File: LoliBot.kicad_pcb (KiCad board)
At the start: 2 copper layers, 146 x 100 mm, 27 parts, among them J1 LOLINBATT, J10 LEFT-MOTOR, J2 APA106, J3 SERVO1, J4 RIGHT, J5 LEFT, J6 MPU-9250, J7 APA106, J8 APA106, J9 RIGHT-MOTOR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

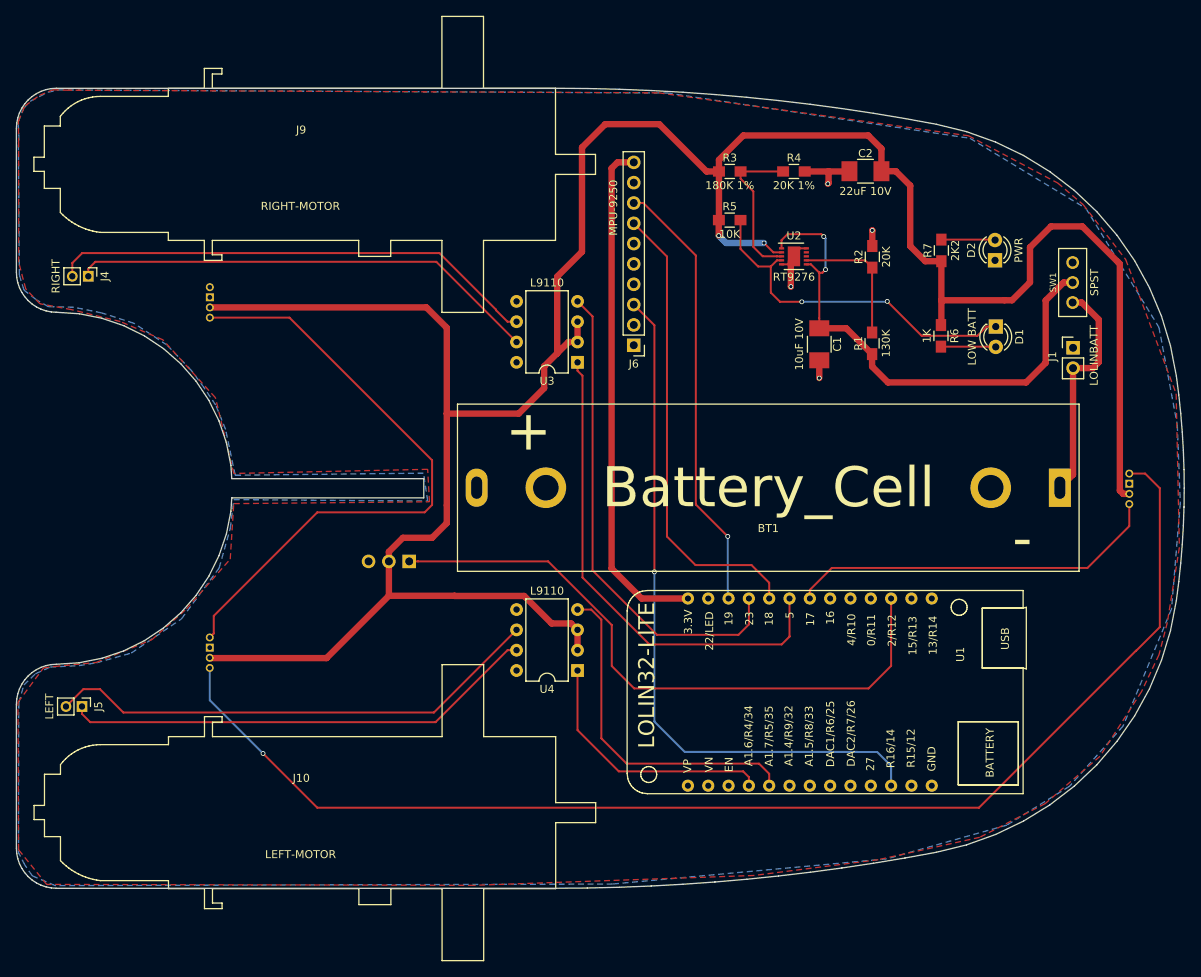
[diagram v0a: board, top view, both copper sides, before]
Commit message: Added Mounting brackets and IR sensor
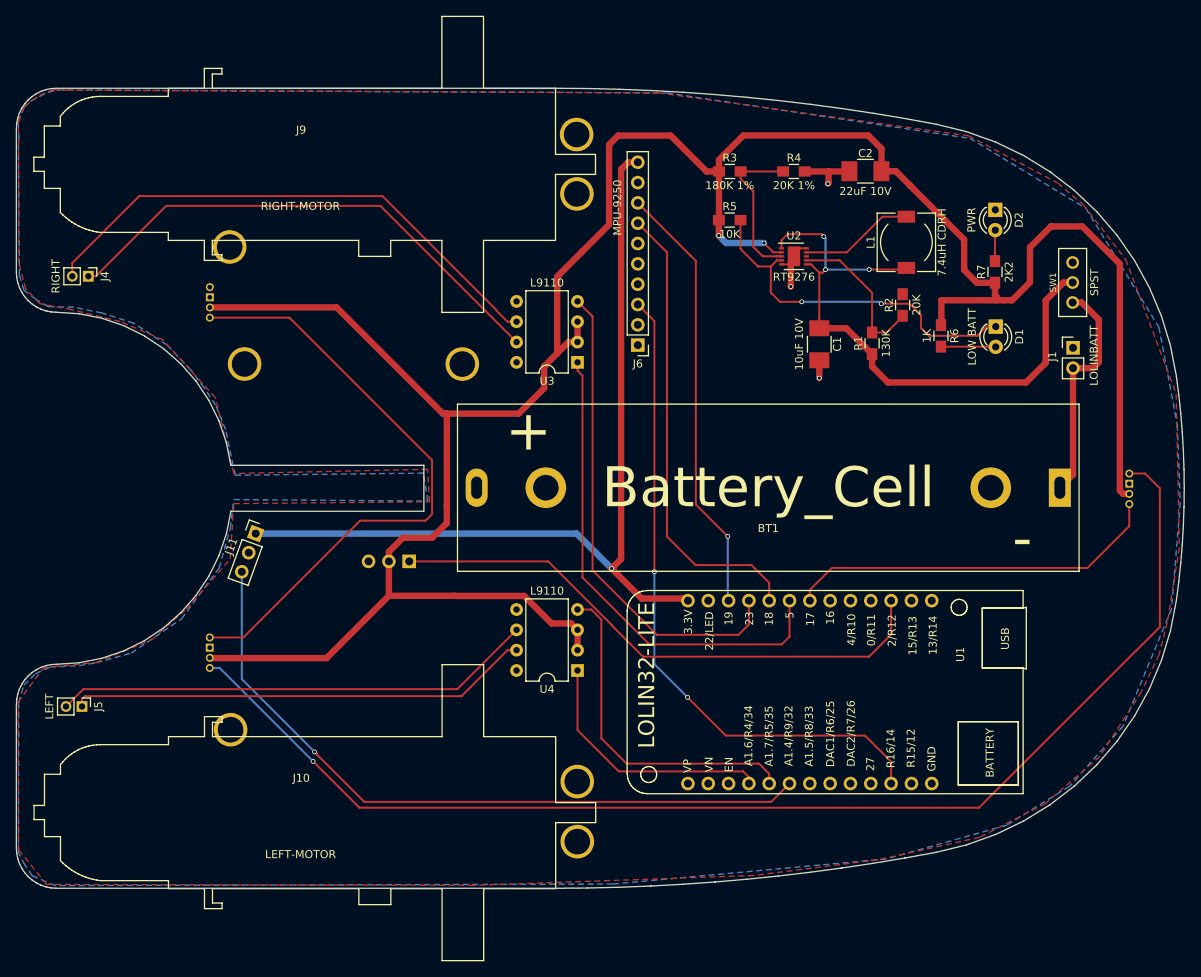
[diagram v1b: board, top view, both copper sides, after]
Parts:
- added J11: REFLECT_, Pin_Headers:Pin_Header_Straight_1x03_Pitch2.54mm, F.Cu at (80.9, 94.9)
- added J12: MECH, Mounting_Holes:MountingHole_3.2mm_M3_Pad, F.Cu at (106.7, 73.7)
- added J13: MECH, Mounting_Holes:MountingHole_3.2mm_M3_Pad, F.Cu at (121.1, 125.9)
- added J14: MECH, Mounting_Holes:MountingHole_3.2mm_M3_Pad, F.Cu at (121.1, 133.4)
- added J15: MECH, Mounting_Holes:MountingHole_3.2mm_M3_Pad, F.Cu at (79.5, 73.7)
- added J16: MECH, Mounting_Holes:MountingHole_3.2mm_M3_Pad, F.Cu at (77.8, 119.4)
- added J17: MECH, Mounting_Holes:MountingHole_3.2mm_M3_Pad, F.Cu at (77.6, 59.1)
- added J18: MECH, Mounting_Holes:MountingHole_3.2mm_M3_Pad, F.Cu at (121.0, 52.5)
- added J19: MECH, Mounting_Holes:MountingHole_3.2mm_M3_Pad, F.Cu at (121.0, 45.0)
- added L1: 7.4uH CDRH, Choke_SMD:Choke_SMD_7.3x7.3_H3.5, F.Cu at (162.2, 58.5)
- moved R7 7.22 mm to (173.3, 62.2)
- moved R2 7.11 mm to (161.8, 66.4)
- moved D2 6.31 mm to (173.3, 54.5), turned to 270 degrees
- moved J6 0.51 mm to (128.7, 71.4)
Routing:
- net /IO32: track 0.00 -> 89.2 mm, vias 0 -> 1
- net +3V3: track 64.2 -> 110.2 mm, vias 0 -> 1
- net Net-(L1-Pad2): track 0.00 -> 14.3 mm
- net Net-(C1-Pad1): track 66.1 -> 76.3 mm, vias 2 -> 3
- net /IO2: track 79.4 -> 70.9 mm
- net +5V: track 322.8 -> 316.4 mm
- net Net-(J4-Pad2): track 61.3 -> 67.2 mm
- net Net-(J4-Pad1): track 59.0 -> 64.2 mm
- net /INT: track 87.5 -> 83.2 mm, vias 1 -> 2
- net Net-(R1-Pad2): track 16.7 -> 19.6 mm
- net Net-(D2-Pad2): track 6.73 -> 3.89 mm
- net Net-(J5-Pad2): track 62.7 -> 60.3 mm
- net Net-(J2-Pad4): track 159.6 -> 157.3 mm
- net GND: track 20.0 -> 18.0 mm, vias 4 -> 3
- net Net-(J5-Pad1): track 59.4 -> 57.8 mm
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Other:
- outline, holes or cut-outs redrawn

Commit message: Updated footprint
Improved motor driver positions.
Rotated acel to match x/y directions
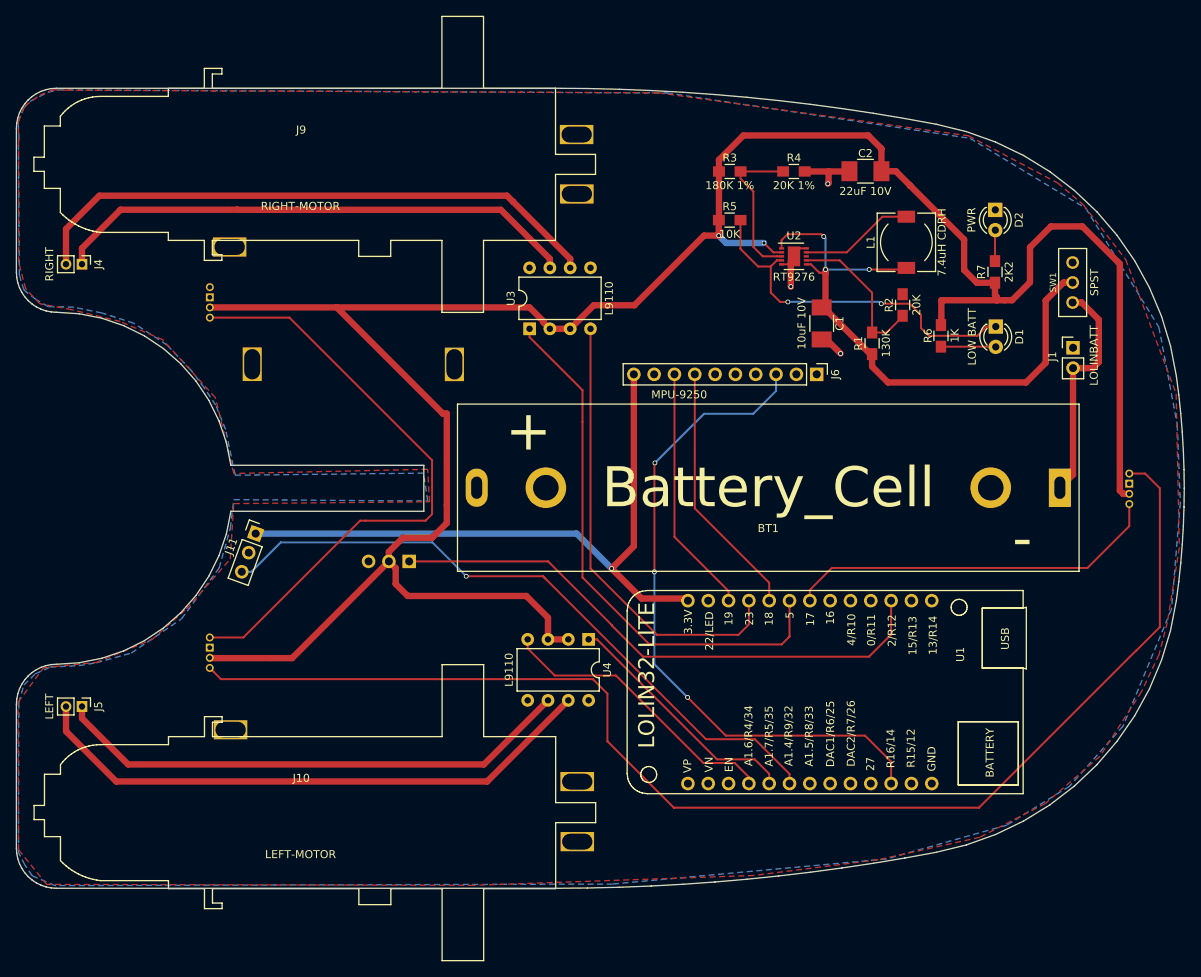
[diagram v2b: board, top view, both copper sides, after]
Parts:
- moved J6 22.7 mm to (151.0, 75.0), turned to 270 degrees
- moved U3 7.32 mm to (115.1, 69.3), turned to 90 degrees
- moved U4 4.13 mm to (122.5, 108.1), turned to 270 degrees
- moved C1 2.62 mm to (151.6, 68.7)
- moved J4 1.70 mm to (59.2, 61.3)
- moved J12 0.99 mm to (105.7, 73.8)
- moved J15 0.96 mm to (80.5, 73.8)
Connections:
- U4 pad 1: /IO34 -> /IO35
- U4 pad 4: /IO35 -> /IO34
- U4 pad 6: Net-(J5-Pad2) -> Net-(J5-Pad1)
- U4 pad 7: Net-(J5-Pad1) -> Net-(J5-Pad2)
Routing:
- net +3V3: track 110.2 -> 82.8 mm
- net /IO18: track 57.8 -> 31.9 mm
- net /IO19: track 54.2 -> 31.2 mm, vias 1 -> 0
- net +5V: track 316.4 -> 300.0 mm
- net Net-(J5-Pad2): track 60.3 -> 72.7 mm
- net /IO35: track 42.6 -> 31.0 mm
- net Net-(J5-Pad1): track 57.8 -> 65.4 mm
- net /IO5: track 61.7 -> 68.3 mm
- net Net-(J4-Pad2): track 67.2 -> 73.5 mm
- net /IO32: track 89.2 -> 83.4 mm
- net /IO34: track 32.4 -> 36.5 mm
- net /IO23: track 61.1 -> 57.0 mm
- net Net-(J2-Pad4): track 157.3 -> 160.8 mm, vias 1 -> 0
- net Net-(J4-Pad1): track 64.2 -> 66.1 mm
- net Net-(C1-Pad1): track 76.3 -> 75.1 mm
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
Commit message: Whoops, those L9110 Pins don't go there.
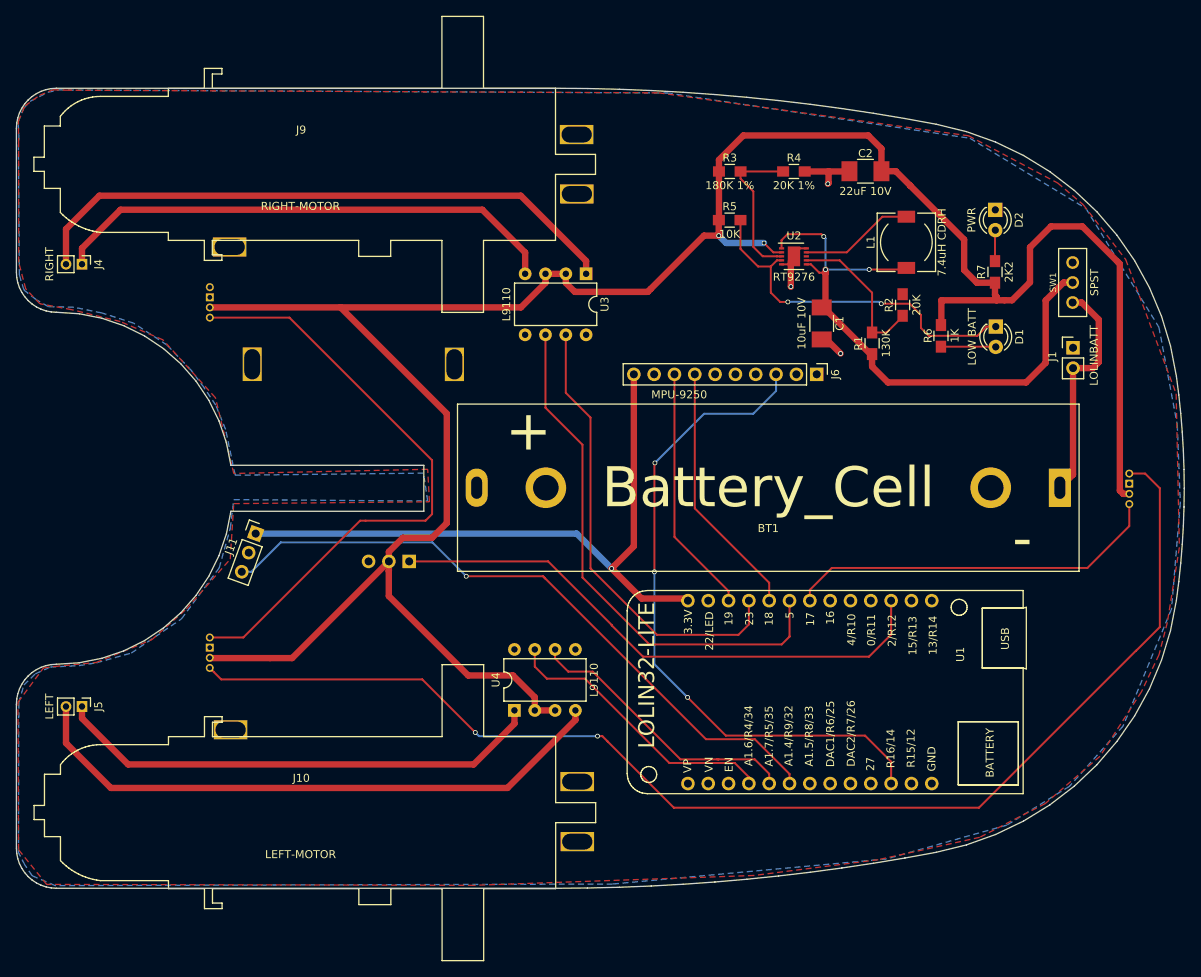
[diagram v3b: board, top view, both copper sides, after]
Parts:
- moved U4 12.8 mm to (113.2, 117.0), turned to 90 degrees
- moved U3 9.86 mm to (122.2, 62.5), turned to 270 degrees
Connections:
- U3 pad 1: /IO5 -> Net-(J4-Pad2)
- U3 pad 4: /IO23 -> Net-(J4-Pad1)
- U3 pad 6: Net-(J4-Pad2) -> /IO5
- U3 pad 7: Net-(J4-Pad1) -> /IO23
- U4 pad 1: /IO35 -> Net-(J5-Pad1)
- U4 pad 4: /IO34 -> Net-(J5-Pad2)
- U4 pad 6: Net-(J5-Pad1) -> /IO35
- U4 pad 7: Net-(J5-Pad2) -> /IO34
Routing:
- net /IO35: track 31.0 -> 35.5 mm
- net Net-(J5-Pad1): track 65.4 -> 61.7 mm
- net Net-(J2-Pad4): track 160.8 -> 157.3 mm, vias 0 -> 2
- net +5V: track 300.0 -> 303.2 mm
- net Net-(J5-Pad2): track 72.7 -> 75.3 mm
- net Net-(J4-Pad2): track 73.5 -> 76.1 mm
- net Net-(J4-Pad1): track 66.1 -> 64.3 mm
- net /IO5: track 68.3 -> 66.8 mm
- net /IO34: track 36.5 -> 35.7 mm
- net /IO23: track 57.0 -> 57.5 mm

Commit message: Pin reassignment.
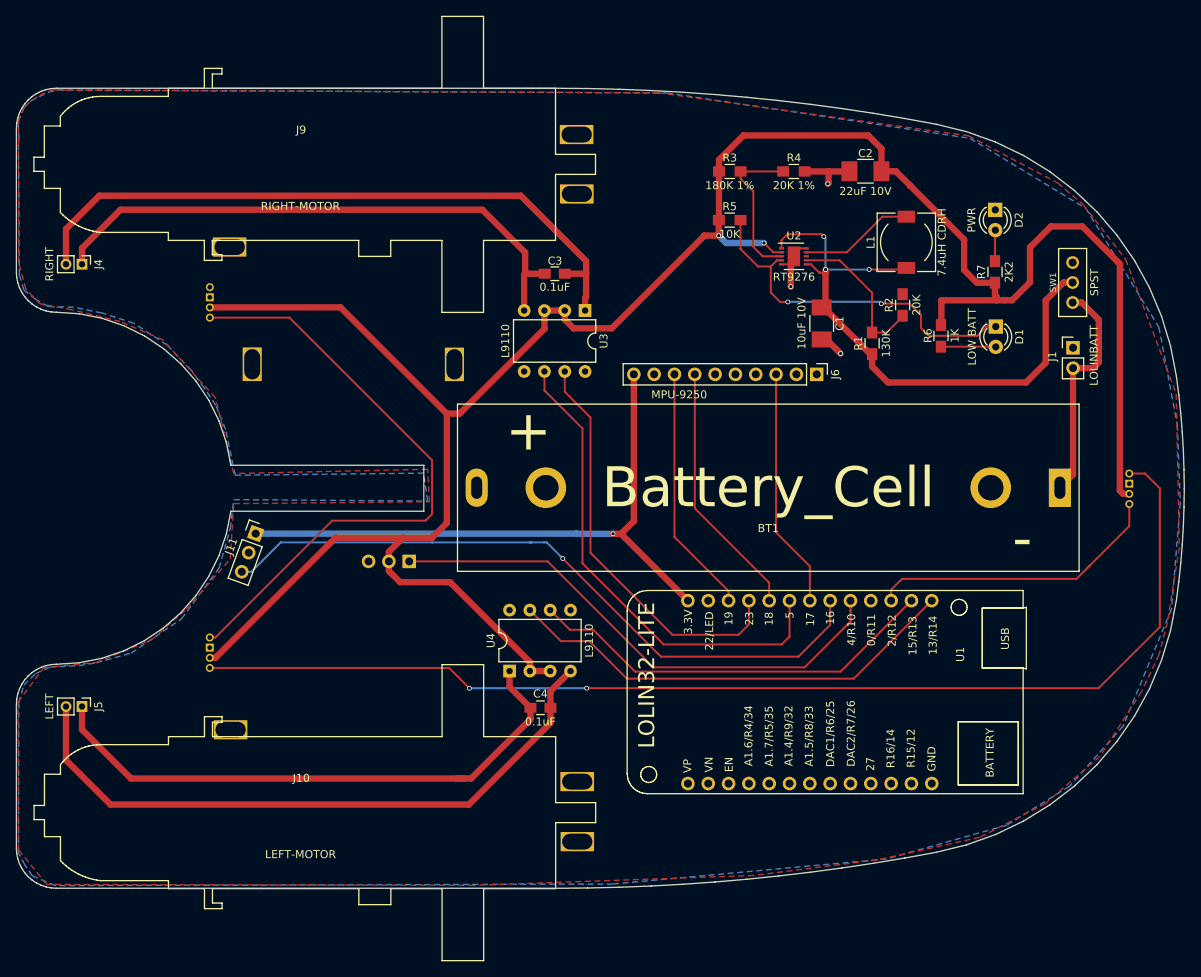
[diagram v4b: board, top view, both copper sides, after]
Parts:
- added C3: 0.1uF, Capacitors_SMD:C_0805_HandSoldering, F.Cu at (118.3, 62.4)
- added C4: 0.1uF, Capacitors_SMD:C_0805_HandSoldering, F.Cu at (116.5, 116.7)
- moved U4 4.96 mm to (112.6, 112.1)
- moved U3 4.59 mm to (122.1, 67.0)
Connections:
- J11 pad 3: /IO32 -> /IO16
- J2 pad 1: /IO17 -> /IO2
- J3 pad 1: /IO2 -> /IO4
- U1 pad 11: /INT -> /IO14
- U1 pad 20: /IO17 -> /INT
- U4 pad 6: /IO35 -> /IO15
- U4 pad 7: /IO34 -> /IO13
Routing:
- net /IO16: track 0.00 -> 85.9 mm, vias 0 -> 1
- net /IO32: track 83.4 -> 0.00 mm, vias 1 -> 0
- net /IO4: track 0.00 -> 65.6 mm
- net /IO13: track 0.00 -> 57.8 mm
- net /INT: track 83.5 -> 30.0 mm, vias 3 -> 0
- net /IO15: track 0.00 -> 52.0 mm
- net /IO17: track 47.1 -> 0.00 mm
- net /IO35: track 35.5 -> 0.00 mm
- net /IO34: track 35.7 -> 1.08 mm
- net /IO2: track 70.9 -> 37.6 mm
- net Net-(J2-Pad4): track 157.3 -> 144.9 mm
- net Net-(C4-Pad1): track 61.7 -> 72.6 mm
- net +5V: track 303.2 -> 294.4 mm
- net Net-(C3-Pad1): track 76.1 -> 83.4 mm
- net Net-(C3-Pad2): track 64.3 -> 71.5 mm
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
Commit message: Added expansion ports
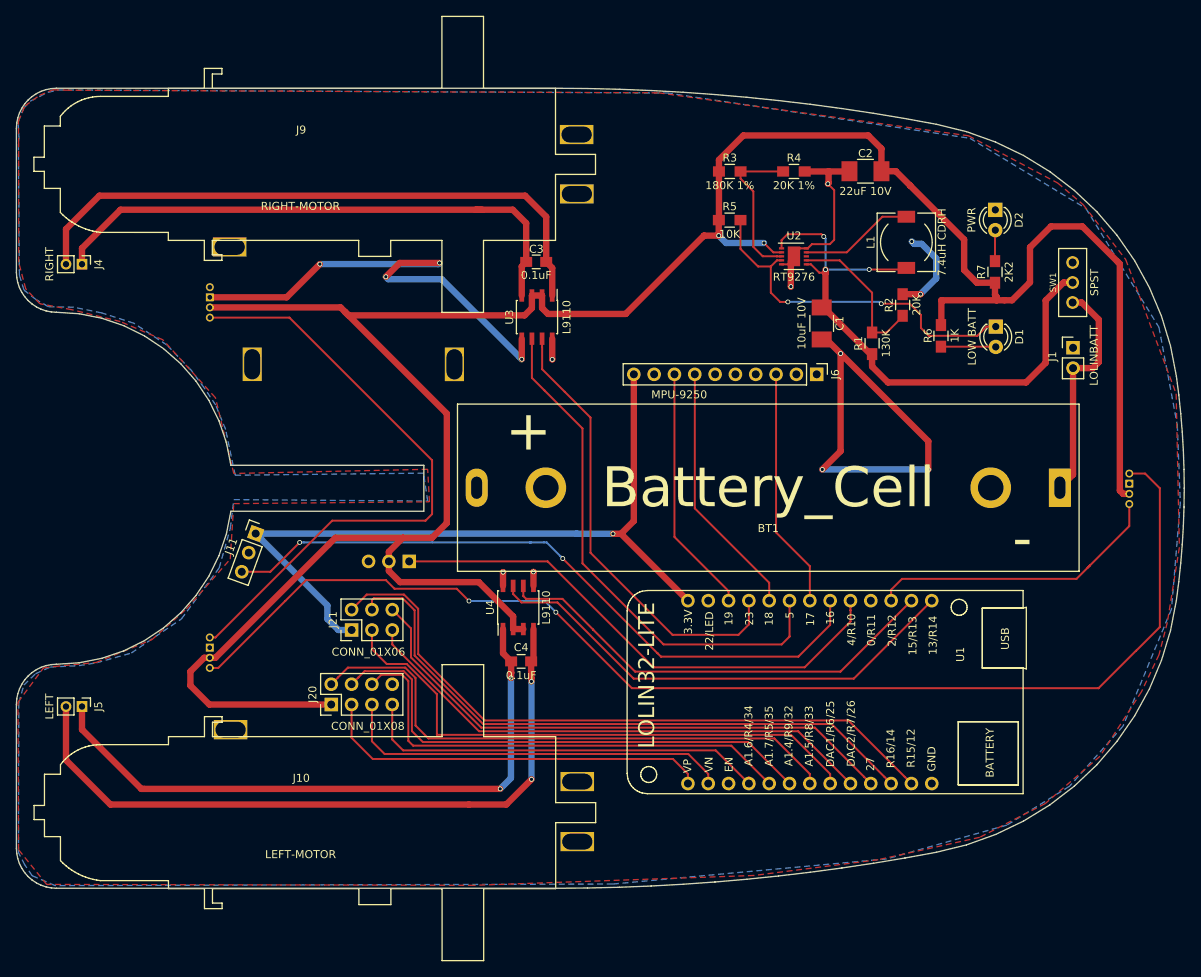
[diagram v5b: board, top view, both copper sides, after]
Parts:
- added J20: CONN_01X08, Pin_Headers:Pin_Header_Straight_2x04_Pitch2.54mm, F.Cu at (90.3, 116.3)
- added J21: CONN_01X06, Pin_Headers:Pin_Header_Straight_2x03_Pitch2.54mm, F.Cu at (92.9, 107.0)
- U3, U4: footprint Housings_DIP:DIP-8_W7.62mm -> Housings_SOIC:SOIC-8_3.9x4.9mm_Pitch1.27mm
- moved U4 8.02 mm to (113.7, 104.2)
- moved C4 6.28 mm to (114.1, 110.9)
- moved U3 6.07 mm to (116.1, 67.9)
- moved C3 2.76 mm to (116.0, 61.0)
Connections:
- net /FN renamed /EN
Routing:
- net GND: track 18.9 -> 157.1 mm, vias 3 -> 14
- net /IO12: track 0.00 -> 83.9 mm
- net /IO14: track 0.00 -> 79.1 mm
- net /IO27: track 0.00 -> 70.9 mm
- net /IO33: track 0.00 -> 70.9 mm
- net /IO25: track 0.00 -> 70.3 mm
- net /IO26: track 0.00 -> 66.3 mm
- net /IO32: track 0.00 -> 65.0 mm
- net /IO35: track 0.00 -> 60.2 mm
- net /IO34: track 1.08 -> 52.3 mm
- net /VN: track 0.00 -> 49.5 mm
- net /VP: track 0.00 -> 49.3 mm
- net +5V: track 294.4 -> 320.3 mm
- net +3V3: track 78.1 -> 96.1 mm
- net Net-(J2-Pad4): track 144.9 -> 154.0 mm
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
